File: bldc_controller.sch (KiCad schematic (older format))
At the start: 151 parts, among them J1 Conn_01x06_Male, J2 Screw_Terminal_01x04, Q1 2N7002E, Q10 IRLB8721PBF, Q11 IRLB8721PBF, Q2 DMN65D8L-7, Q3 DMN65D8L-7, Q4 MMBT3904, Q5 IRF4905, Q6 IRLB8721PBF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

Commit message: Just Need to Fix Silkscreen
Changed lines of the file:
@@
 F 3 "~" H 8950 9800 50  0001 C CNN
 	1    8950 9800
-	-1   0    0    -1
+	-1   0    0    1
 $EndComp
 Wire Wire Line

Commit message: Just Need to Fix Bottom Silkscreen
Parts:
- renumbered TP12 to TP1
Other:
- moved on the sheet: D1, D3, D4, D6, R1, R10, R3, R5

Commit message: Need to check if output vias are plated
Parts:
- added TP12, TP17, TP18, TP29: TestPoint, TestPoint:TestPoint_Keystone_5000-5004_Miniature, symbol Connector:TestPoint
- added TP19, TP20, TP21, TP22, TP23, TP24, TP25, TP26, TP27, TP28, TP30: TestPoint, TestPoint:TestPoint_THTPad_1.0x1.0mm_Drill0.5mm, symbol Connector:TestPoint
- RV1: value 100K -> 5K; footprint Potentiometer_THT:Potentiometer_Bourns_3339P_Vertical_HandSoldering -> Potentiometer_SMD:Trimmer_Pot_SM
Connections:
- net labels added: ANALOG_IN
- wire segments 299 -> 306
- no-connect marks 8 -> 7

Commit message: Added Preliminary BOMs
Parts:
- D5: Color Red -> Green
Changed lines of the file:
@@
 F 2 "LED_SMD:LED_0805_2012Metric_Pad1.15x1.40mm_HandSolder" H 2250 9350 50  0001 C CNN
 F 3 "~" H 2250 9350 50  0001 C CNN
-F 4 "Red" V 2200 9500 50  0000 C CNN "Color"
+F 4 "Green" V 2200 9550 50  0000 C CNN "Color"
 	1    2250 9350
 	0    -1   -1   0

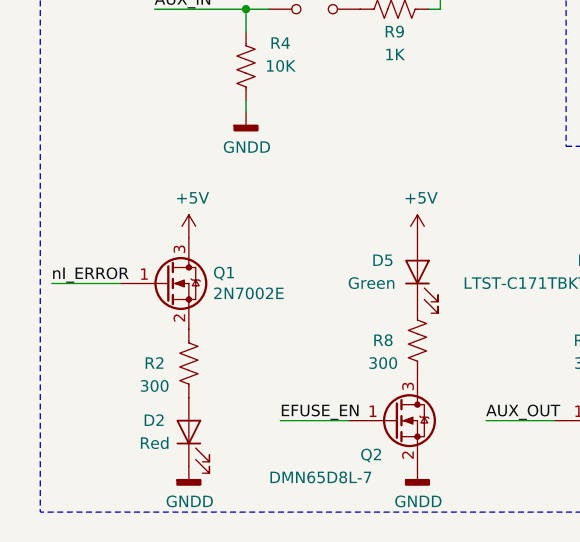
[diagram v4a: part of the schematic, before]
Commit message: Fixed PMOS footprint
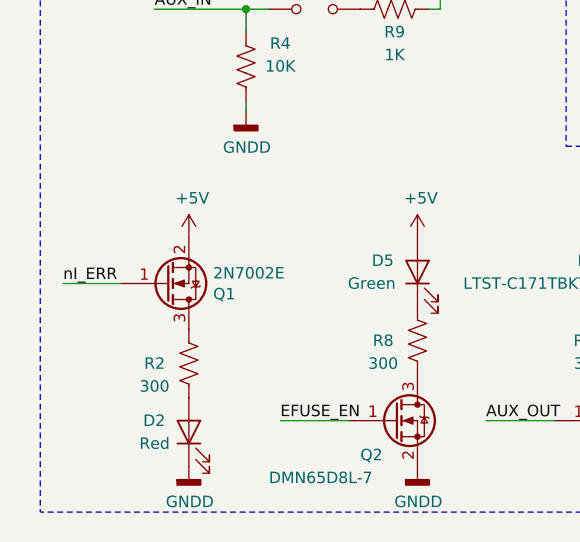
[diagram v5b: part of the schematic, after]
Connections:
- net labels removed: nI_ERROR
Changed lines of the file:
@@
 NoConn ~ 8050 5100
 NoConn ~ 6500 4500
-Wire Wire Line
-	950  9400 650  9400
 $Comp
 L power:GNDD #PWR04
@@
 	1    0    0    -1
 $EndComp
-Text Label 650  9400 0    50   ~ 0
-nI_ERROR
+Text Label 700  9400 0    50   ~ 0
+nI_ERR
 $Comp
 L power:+5V #PWR018
@@
 F 3 "http://www.diodes.com/assets/Datasheets/ds30376.pdf" H 1150 9400 50  0001 L CNN
 	1    1150 9400
-	1    0    0    -1
+	1    0    0    1
 $EndComp
 NoConn ~ 5200 9350
@@
 Text Label 1150 2800 0    50   ~ 0
 ANALOG_IN
+Wire Wire Line
+	700  9400 950  9400
 $EndSCHEMATC
